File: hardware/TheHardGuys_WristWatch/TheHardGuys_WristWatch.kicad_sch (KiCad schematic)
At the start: 7 parts, among them P1 MB102 Output

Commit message: Passed ERC Tests
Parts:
- added C2: 47 uC, Capacitor_THT:CP_Radial_D6.3mm_P2.50mm, symbol Device:C
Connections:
- net +3.3V: now also P1.3 (3.3V), C2.1
- net GND: now also P1.4 (GND), C2.2
- no-connect marks 0 -> 38

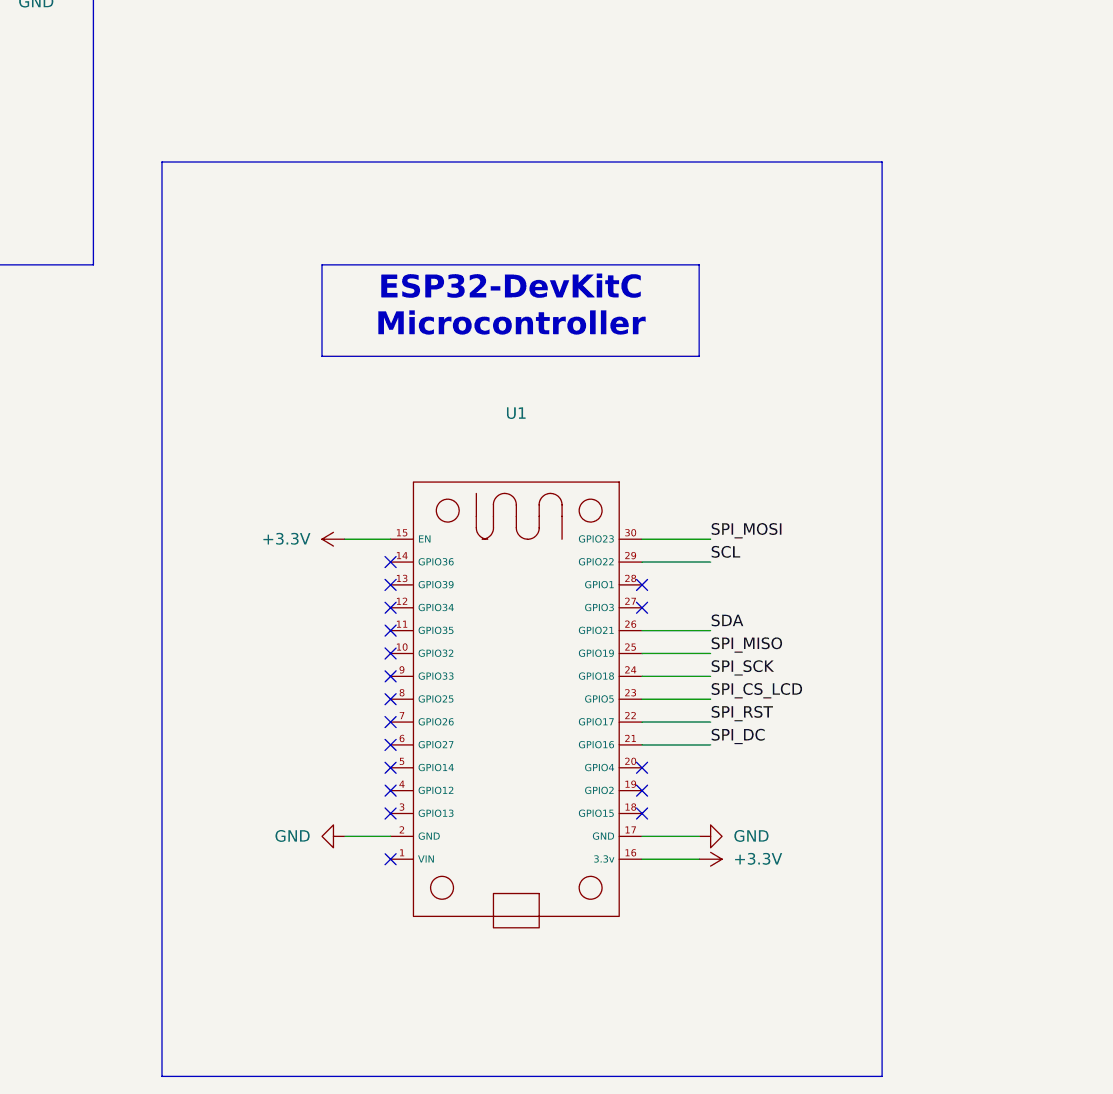
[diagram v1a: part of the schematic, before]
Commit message: Schematic Edited with EPS32 Feather V2. PCB Not updated
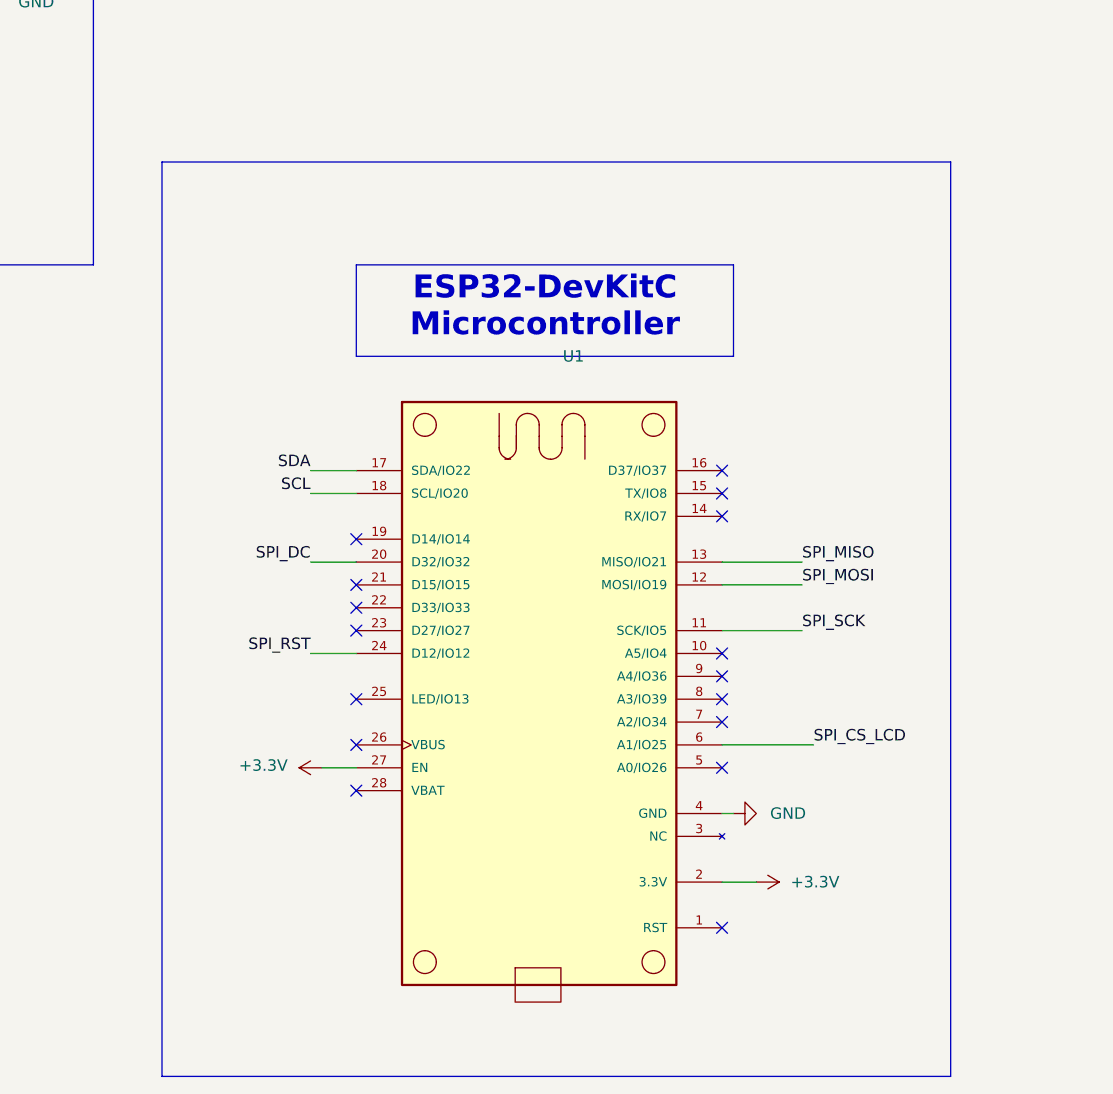
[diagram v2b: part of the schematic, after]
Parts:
- U1: footprint THG_Wristwatch:ESP32_30pin -> THG_Wristwatch:ESP32_Feather_V2; symbol esp32_30pin_revised:ESP32_30Pin -> ESP32_Feather_V2:ESP32_Feather_V2
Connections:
- net +3.3V: now also U1.2 (3.3V), U1.27 (EN); no longer U1.15 (EN), U1.16 (3.3v)
- net GND: now also U1.4 (GND); no longer U1.17 (GND), U1.2 (GND)
- net SCL: now also U1.18 (SCL/IO20); no longer U1.29 (GPIO22)
- net SDA: now also U1.17 (SDA/IO22); no longer U1.26 (GPIO21)
- net SPI_CS_LCD: now also U1.6 (A1/IO25); no longer U1.23 (GPIO5)
- net SPI_DC: now also U1.20 (D32/IO32); no longer U1.21 (GPIO16)
- net SPI_MISO: now also U1.13 (MISO/IO21); no longer U1.25 (GPIO19)
- net SPI_MOSI: now also U1.12 (MOSI/IO19); no longer U1.30 (GPIO23)
- net SPI_RST: now also U1.24 (D12/IO12); no longer U1.22 (GPIO17)
- net SPI_SCK: now also U1.11 (SCK/IO5); no longer U1.24 (GPIO18)
- no-connect marks 38 -> 36
